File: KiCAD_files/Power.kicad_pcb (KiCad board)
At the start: 2 copper layers, 90 x 100 mm, 92 parts, among them J1 2604-1102, J2 2604-1102, J3 Power_Board_outline, J4 2604-1102, J5 2604-1102, Q1 QM6006D, Q2 QM6006D, Q3 Q_NIGBT_GCE, Q4 QM6006D, Q5 QM6006D, U1 ACS730xLCTR-20AB, U2 LM35-LP, U3 ACS712xLCTR-20A, U4 ACS730xLCTR-20AB

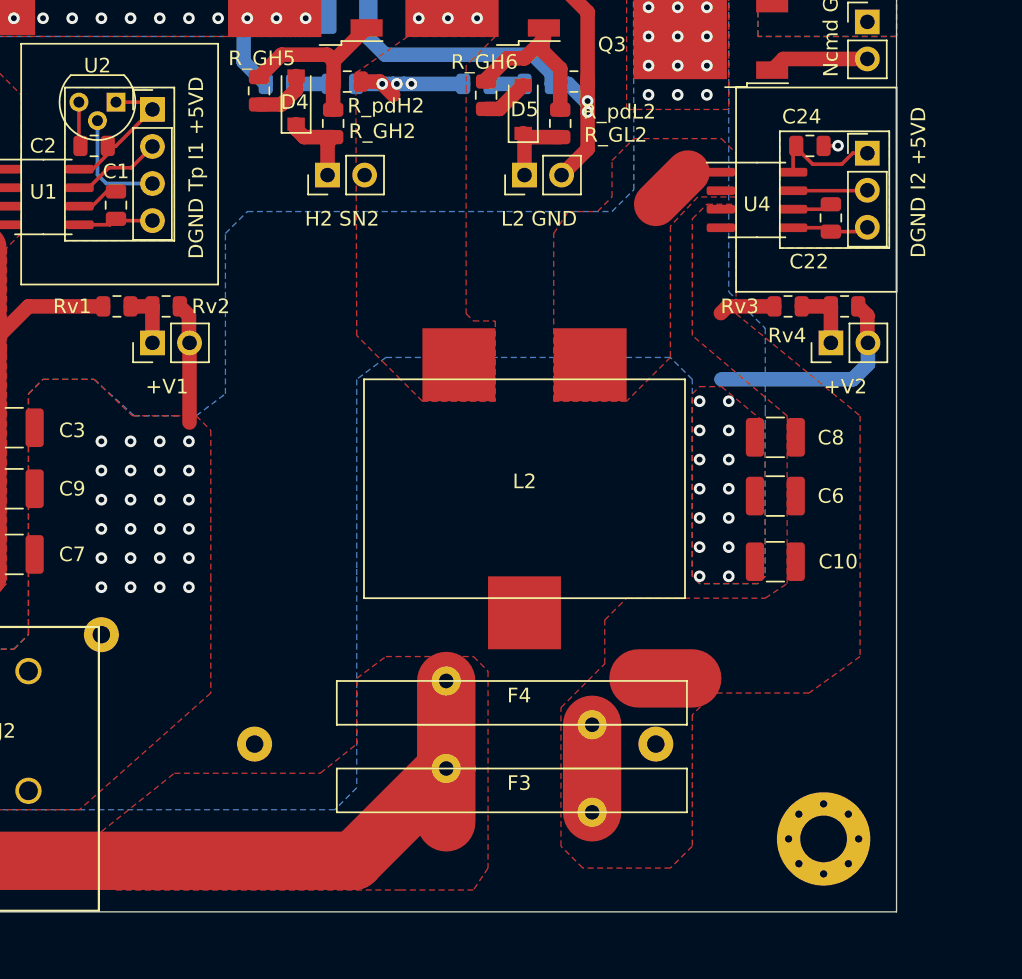
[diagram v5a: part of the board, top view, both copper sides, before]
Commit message: Finalized overlay and added License info and current version Finalized the nucleo shield - added a CR2032 battery holder for the RTC.
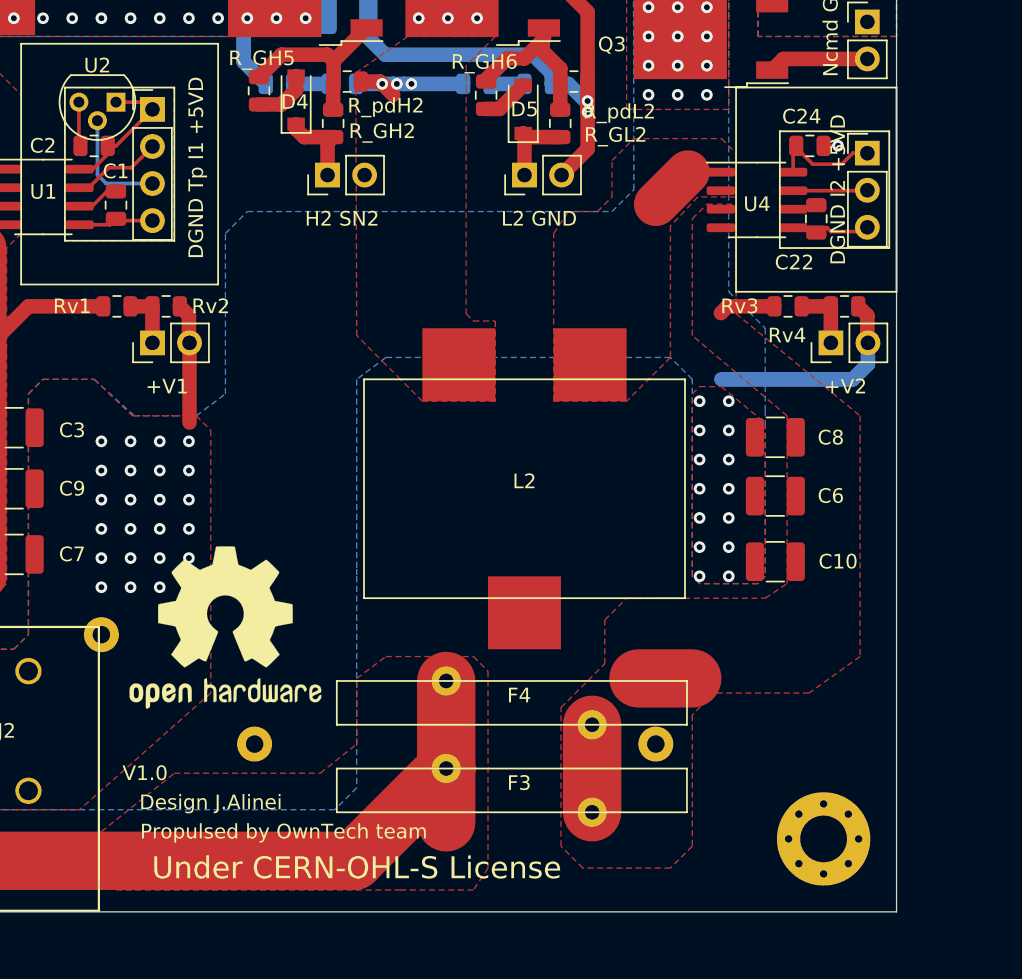
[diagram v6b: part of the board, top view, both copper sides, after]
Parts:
- added REF**: OSHW-Logo2_14.6x12mm_SilkScreen, Symbol:OSHW-Logo2_14.6x12mm_SilkScreen, F.Cu at (86.0, 122.5)
- moved C22 1.00 mm to (126.5, 94.5)
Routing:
- net Net-(C22-Pad1): track 2.73 -> 1.70 mm
- net /DGND: track 21.6 -> 22.5 mm
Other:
- board text added: "Design J.Alinei"
- board text added: "Propulsed by OwnTech team"
- board text added: "Under CERN-OHL-S License"
- board text added: "V1.0"

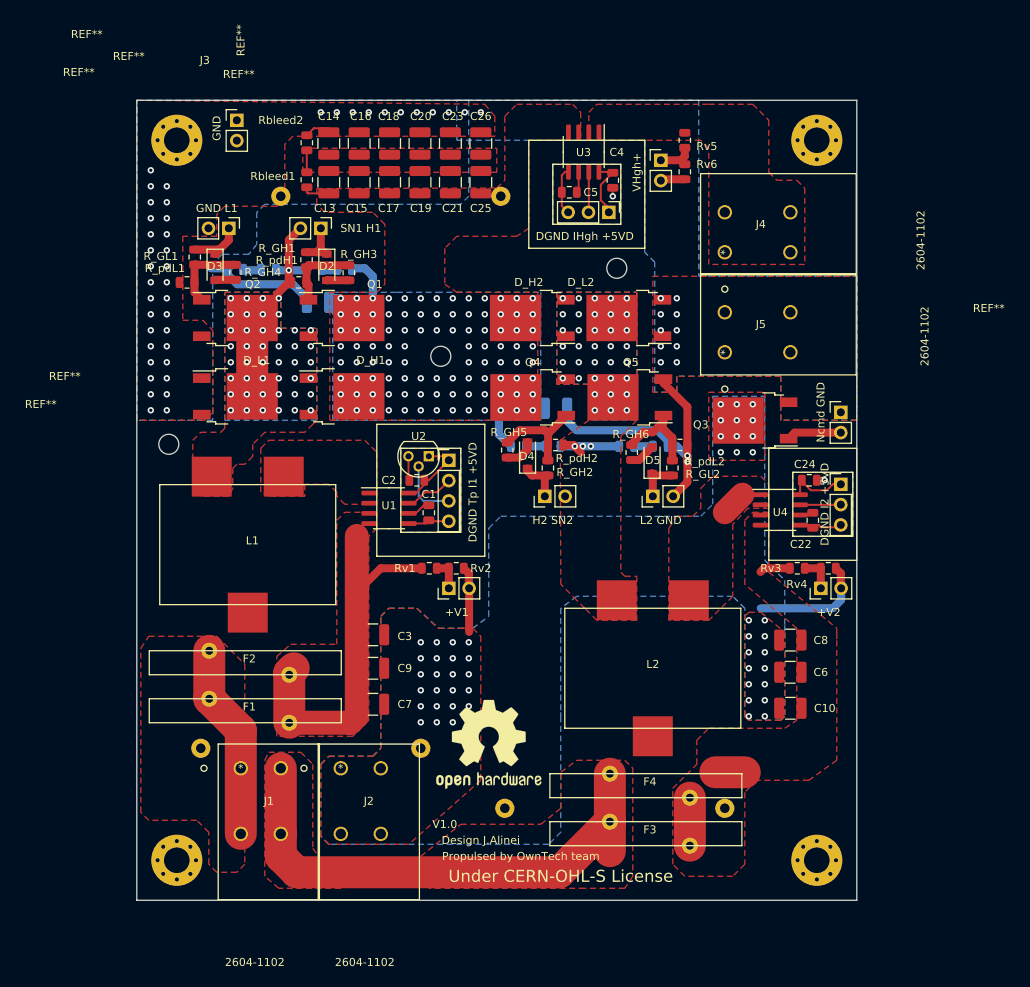
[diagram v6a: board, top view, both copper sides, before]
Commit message: Solved minor glitch on the overlay.
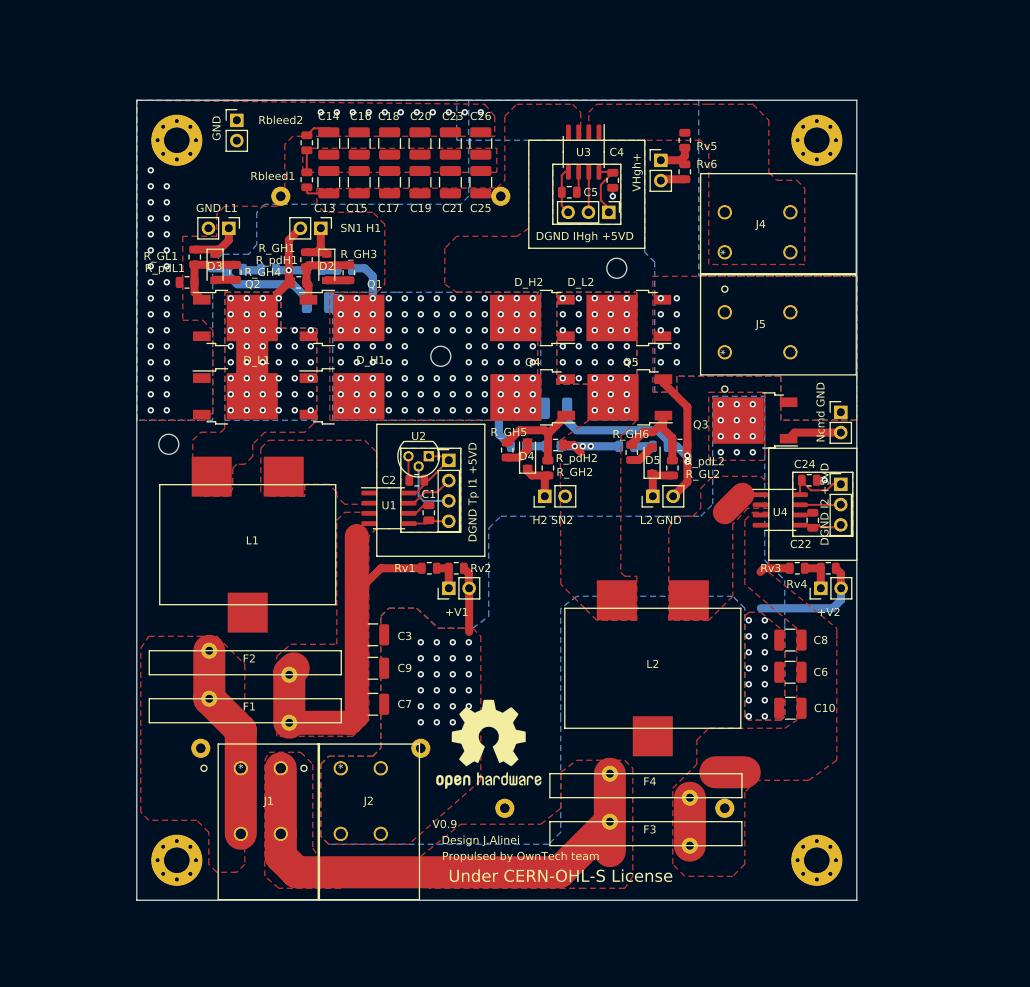
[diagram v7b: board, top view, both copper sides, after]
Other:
- board text added: "V0.9"
- board text removed: "V1.0"

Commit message: Modified power board according to Theo's remarks.
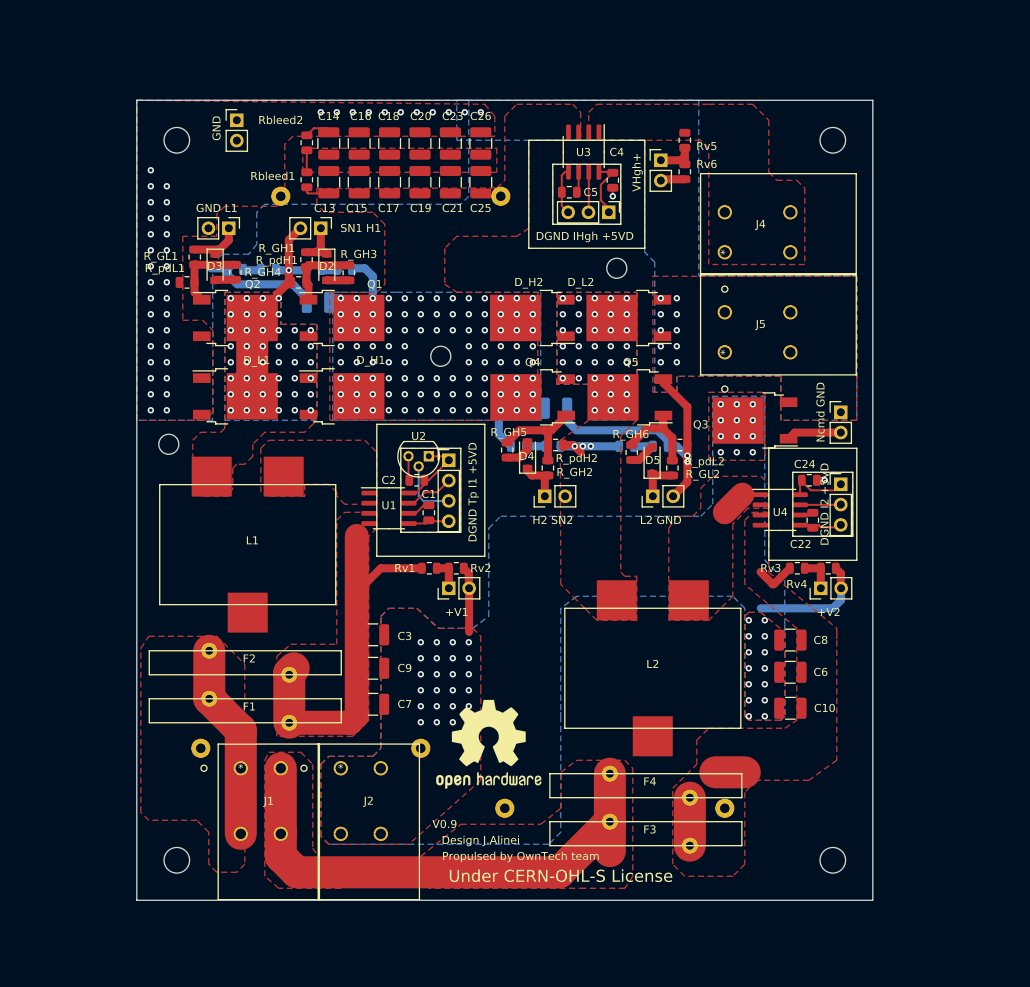
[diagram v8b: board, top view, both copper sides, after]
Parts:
- removed the REF** at (47.0, 47.0)
- removed the REF** at (127.0, 47.0)
- removed the REF** at (47.0, 137.0)
- removed the REF** at (127.0, 137.0)
- added REF**: MountingHole_3.2mm_M3, MountingHole:MountingHole_3.2mm_M3, F.Cu at (129.0, 137.0)
- added REF**: MountingHole_3.2mm_M3, MountingHole:MountingHole_3.2mm_M3, F.Cu at (47.0, 137.0)
- added REF**: MountingHole_3.2mm_M3, MountingHole:MountingHole_3.2mm_M3, F.Cu at (47.0, 47.0)
- added REF**: MountingHole_3.2mm_M3, MountingHole:MountingHole_3.2mm_M3, F.Cu at (129.0, 47.0)
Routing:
- net /V_In2: track 13.5 -> 14.8 mm
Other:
- board size 90 x 100 mm -> 92 x 100 mm
